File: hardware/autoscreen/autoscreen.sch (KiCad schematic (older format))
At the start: 39 parts, among them J1 USB_B_Micro, J2 Conn_01x06_Male, Q1 Q_Photo_NPN_EC, SW1 SW_Push, SW2 SW_Push, U1 AZ1117-3.3, U2 STM32F722RETx, Y1 12MHz

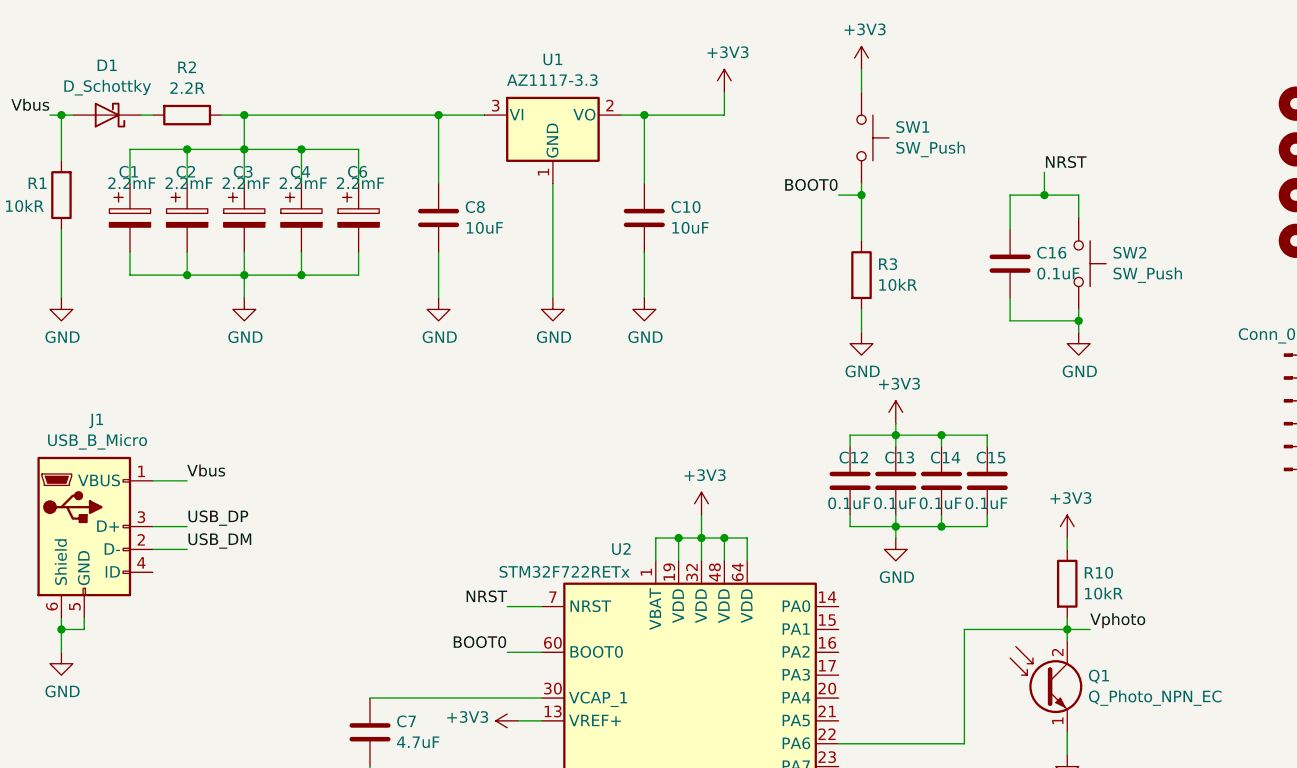
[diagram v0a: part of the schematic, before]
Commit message: Updated input resistor value to limit inrush current
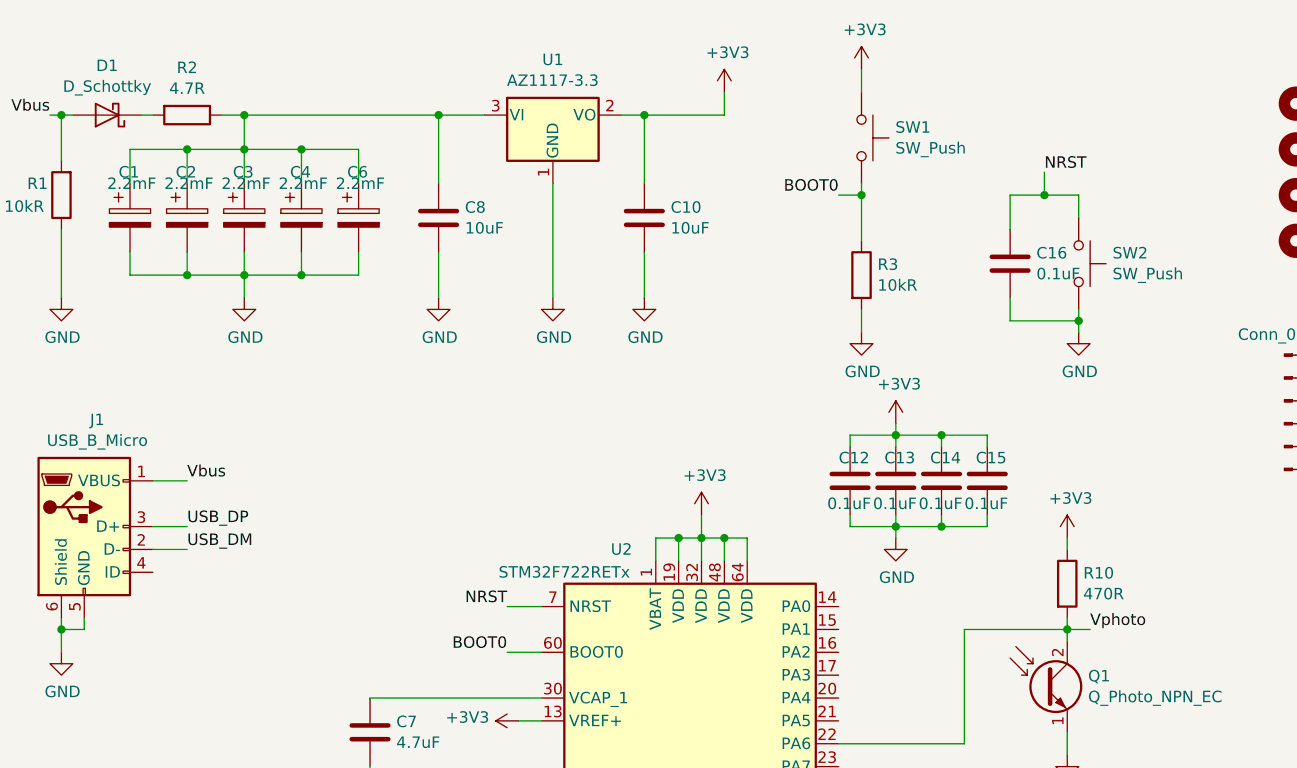
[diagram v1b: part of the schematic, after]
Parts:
- R10: value 10kR -> 470R
- R2: value 2.2R -> 4.7R
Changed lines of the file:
@@
 EESchema Schematic File Version 4
+LIBS:autoscreen-cache
 EELAYER 30 0
 EELAYER END
@@
 P 5250 3150
 F 0 "R10" H 5320 3196 50  0000 L CNN
-F 1 "10kR" H 5320 3105 50  0000 L CNN
+F 1 "470R" H 5320 3105 50  0000 L CNN
 F 2 "Resistor_SMD:R_0805_2012Metric_Pad1.15x1.40mm_HandSolder" V 5180 3150 50  0001 C CNN
 F 3 "~" H 5250 3150 50  0001 C CNN
@@
 P 1400 1100
 F 0 "R2" V 1193 1100 50  0000 C CNN
-F 1 "2.2R" V 1284 1100 50  0000 C CNN
+F 1 "4.7R" V 1284 1100 50  0000 C CNN
 F 2 "Resistor_SMD:R_0805_2012Metric_Pad1.15x1.40mm_HandSolder" V 1330 1100 50  0001 C CNN
 F 3 "~" H 1400 1100 50  0001 C CNN
